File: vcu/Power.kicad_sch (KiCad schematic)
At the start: 21 parts, among them J3 PWR, U11 LD1117S33TR_SOT223, U2 LMR33630CRNX

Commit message: More changes to VCU v2.0.0
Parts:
- added U14: MPS3435GL, symbol SUFST:MP3435GL
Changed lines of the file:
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@@
 		(dnp no)
 		(fields_autoplaced yes)
-		(property "Reference" "#PWR033"
+		(property "Reference" "#PWR0102"
 			(at 198.12 64.77 0)
 			(effects
@@
 			(project "vcu"
 				(path "/d2151cc9-0acc-4d18-a050-63c63ade8261/ef5cbe40-51ae-4964-9d7a-df03e6f84f6f"
-					(reference "#PWR033")
+					(reference "#PWR0102")
 					(unit 1)
 				)
@@
 	)
 	(symbol
+		(lib_id "SUFST:MP3435GL")
+		(at 95.25 95.25 0)
+		(unit 1)
+		(exclude_from_sim no)
+		(in_bom yes)
+		(on_board yes)
+		(dnp no)
+		(property "Reference" "U14"
+			(at 98.806 96.774 0)
+			(effects
+				(font
+					(size 1.27 1.27)
+				)
+			)
+		)
+		(property "Value" "MPS3435GL"
+			(at 99.06 100.076 0)
+			(effects
+				(font
+					(size 1.27 1.27)
+				)
+			)
+		)
+		(property "Footprint" ""
+			(at 95.25 95.25 0)
+			(effects
+				(font
+					(size 1.27 1.27)
+				)
+				(hide yes)
+			)
+		)
+		(property "Datasheet" "https://www.monolithicpower.com/en/documentview/productdocument/index/version/2/document_type/Datasheet/lang/en/sku/MP3435GL"
+			(at 98.806 105.41 0)
+			(effects
+				(font
+					(size 1.27 1.27)
+				)
+				(hide yes)
+			)
+		)
+		(property "Description" ""
+			(at 95.25 95.25 0)
+			(effects
+				(font
+					(size 1.27 1.27)
+				)
+				(hide yes)
+			)
+		)
+		(pin "6"
+		)
+		(pin "10"
+		)
+		(pin "16"
+		)
+		(pin "1"
+		)
+		(pin "11"
+		)
+		(pin "20"
+		)
+		(pin "9"
+		)
+		(pin "7"
+		)
+		(pin "8"
+		)
+		(pin "15"
+		)
+		(pin "19"
+		)
+		(pin "3"
+		)
+		(pin "12"
+		)
+		(pin "17"
+		)
+		(pin "18"
+		)
+		(pin "4"
+		)
+		(pin "5"
+		)
+		(pin "2"
+		)
+		(pin "14"
+		)
+		(pin "13"
+		)
+		(instances
+			(project ""
+				(path "/d2151cc9-0acc-4d18-a050-63c63ade8261/ef5cbe40-51ae-4964-9d7a-df03e6f84f6f"
+					(reference "U14")
+					(unit 1)
+				)
+			)
+		)
+	)
+	(symbol
 		(lib_id "Device:R")
 		(at 242.57 53.34 180)
@@
 		(dnp no)
 		(fields_autoplaced yes)
-		(property "Reference" "#PWR032"
+		(property "Reference" "#PWR0101"
 			(at 242.57 64.77 0)
 			(effects
@@
 			(project "vcu"
 				(path "/d2151cc9-0acc-4d18-a050-63c63ade8261/ef5cbe40-51ae-4964-9d7a-df03e6f84f6f"
-					(reference "#PWR032")
-					(unit 1)
-				)
+					(reference "#PWR0101")
+					(unit 1)
+				)

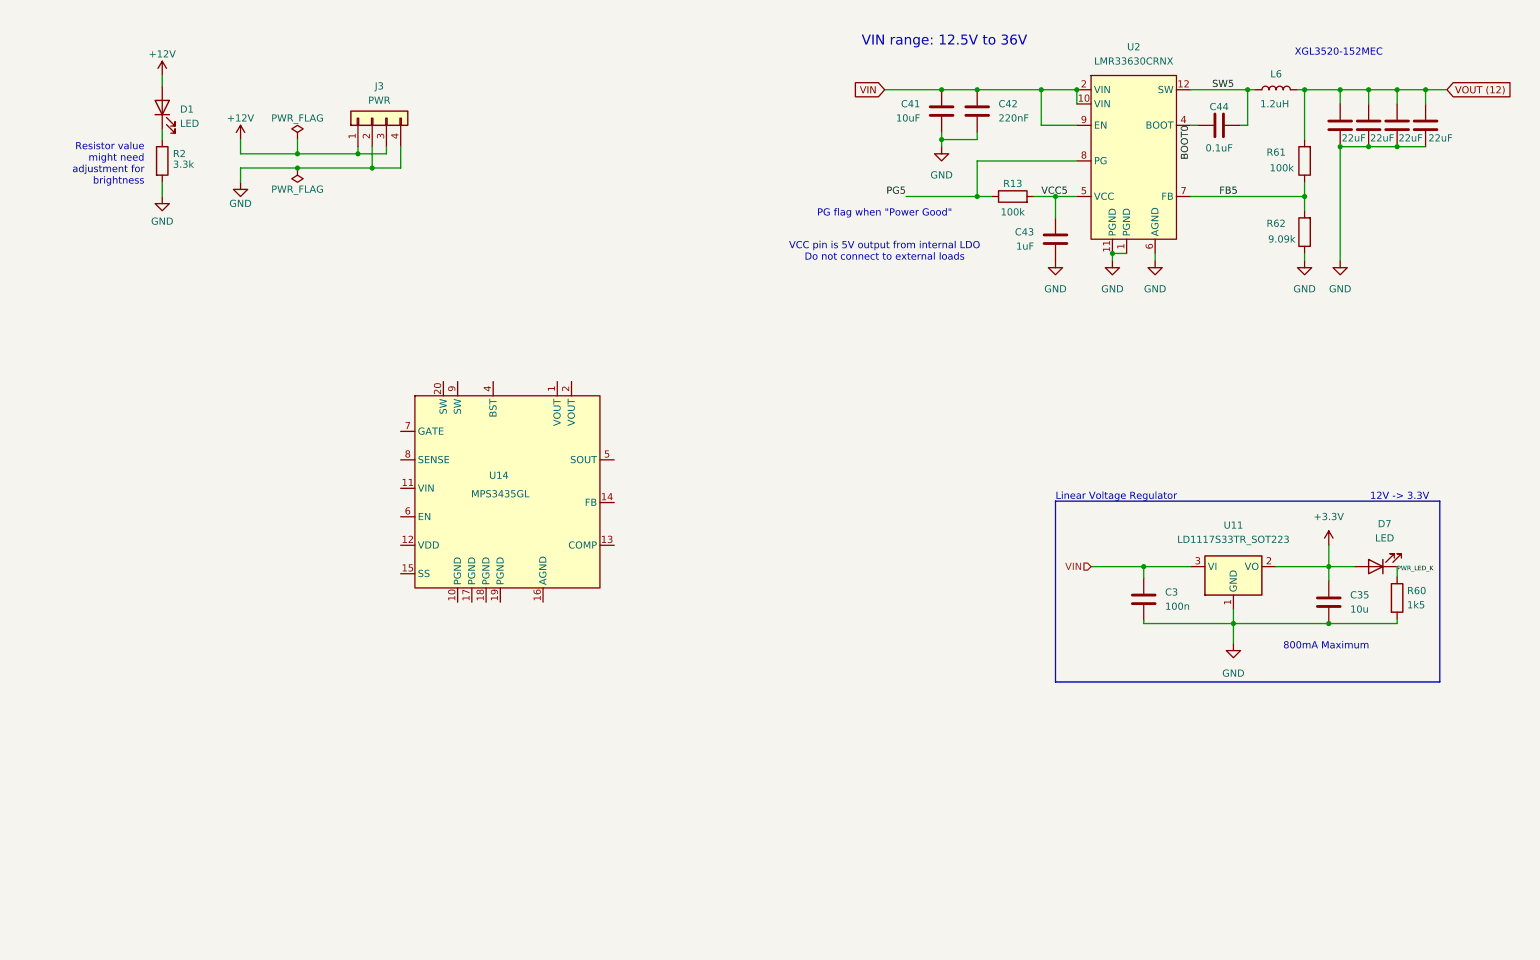
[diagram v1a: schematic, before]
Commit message: Updates to VCU schematic
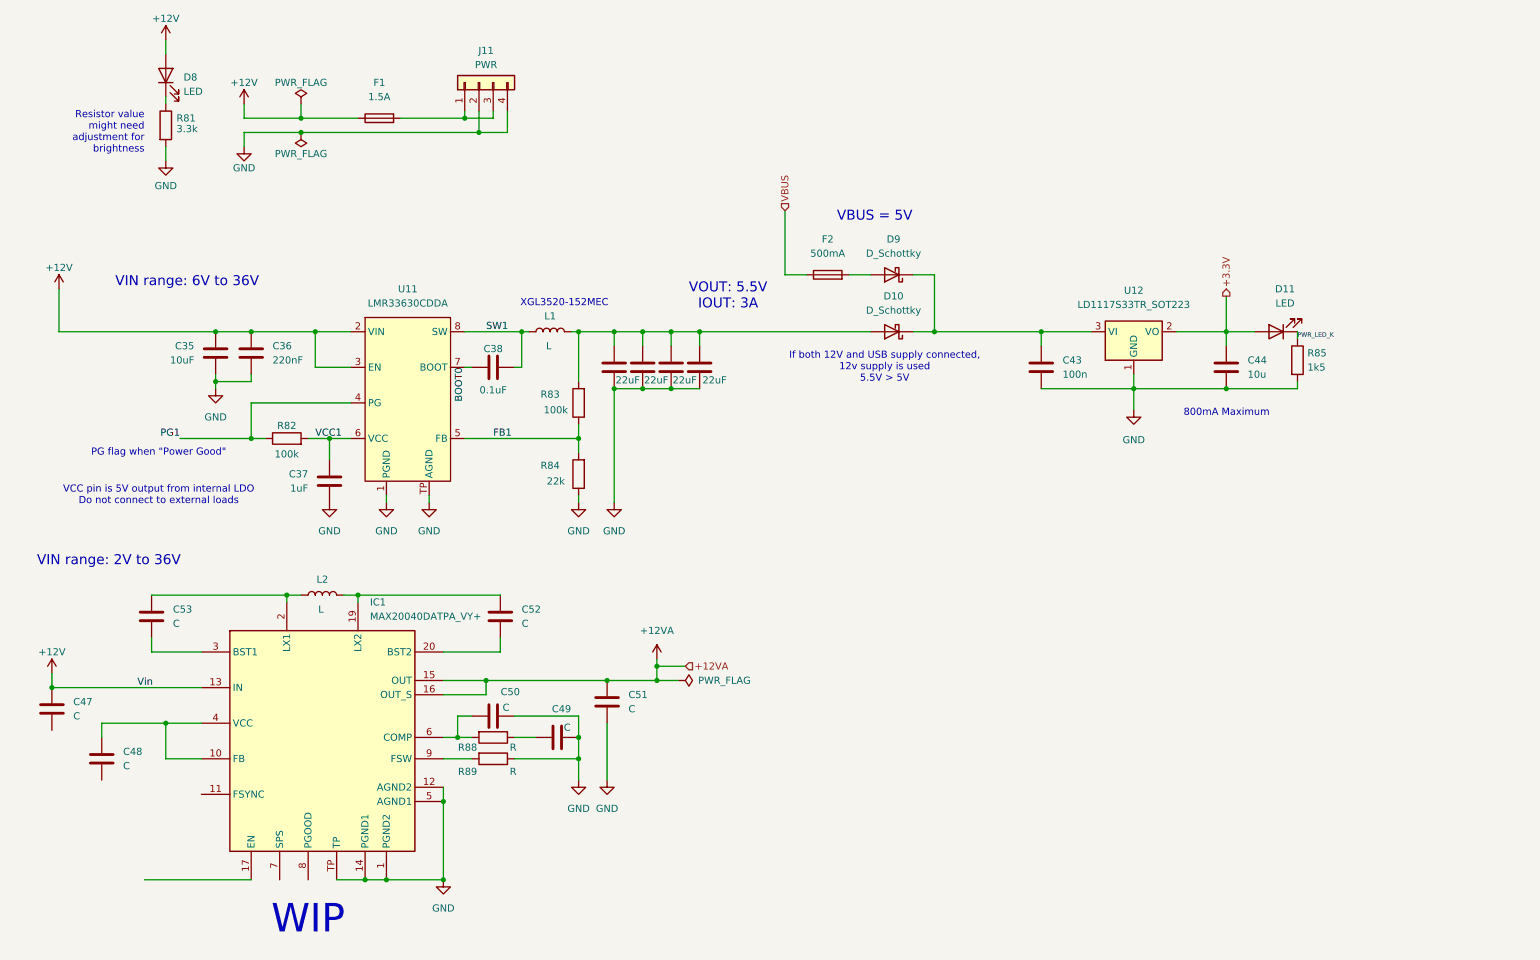
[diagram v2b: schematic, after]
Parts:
- removed C43: 1uF, Capacitor_SMD:C_0603_1608Metric, symbol Device:C
- removed C44: 0.1uF, Capacitor_SMD:C_0603_1608Metric, symbol Device:C
- removed C45, C46: 22uF, Capacitor_SMD:C_0603_1608Metric, symbol Device:C
- removed L6: 1.2uH, SR-Footprint-Library:XGL3520, symbol Device:L
- removed R13, R61: 100k, Resistor_SMD:R_0603_1608Metric, symbol Device:R
- removed R62: 9.09k, Resistor_SMD:R_0603_1608Metric, symbol Device:R
- removed U14: MPS3435GL, symbol SUFST:MP3435GL
- removed U2: LMR33630CRNX, LMR33630CRNX, symbol SR-Symbol-Library:LMR33630CRNX
- added C35: 10uF, Capacitor_SMD:C_0603_1608Metric, symbol Device:C
- added C36: 220nF, Capacitor_SMD:C_0603_1608Metric, symbol Device:C
- added C37: 1uF, Capacitor_SMD:C_0603_1608Metric, symbol Device:C
- added C38: 0.1uF, Capacitor_SMD:C_0603_1608Metric, symbol Device:C
- added C39, C40: 22uF, Capacitor_SMD:C_0603_1608Metric, symbol Device:C
- added C49, C50, C51, C52, C53: C, symbol Device:C
- added D10, D9: D_Schottky, symbol Device:D_Schottky
- added F1: 1.5A, symbol Device:Fuse
- added F2: 500mA, symbol Device:Fuse
- added IC1: MAX20040DATPA_VY+, QFN50P400X400X80-21N-D, symbol SUFST:MAX20040DATPA_VY+
- added L1, L2: L, SR-Footprint-Library:XGL3520, symbol Device:L
- added R82, R83: 100k, Resistor_SMD:R_0603_1608Metric, symbol Device:R
- added R84: 22k, Resistor_SMD:R_0603_1608Metric, symbol Device:R
- added R88, R89: R, symbol Device:R
- added U11: LMR33630CDDA, SR-Footprint-Library:LMR33630CDDA, symbol SR-Symbol-Library:LMR33630CDDA
- C41: value 10uF -> 22uF
- C42: value 220nF -> 22uF
- C47, C48: value 22uF -> C; footprint Capacitor_SMD:C_0603_1608Metric -> (none)
- renumbered C3 to C43, C35 to C44, D7 to D11, D1 to D8, J3 to J11, R2 to R81, R60 to R85, U11 to U12
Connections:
- net +12V: now also C47.1, C35.1, C36.1, F1.1, IC1.13 (IN), U11.2 (VIN), U11.3 (EN); no longer J11.1 (Pin_1), J11.3 (Pin_3)
- net BOOT0: now also C38.1, U11.7 (BOOT)
- net GND: now also C35.2, C36.2, C37.2, C39.2, C40.2, C49.2, C50.2, C51.1, IC1.1 (PGND2), IC1.12 (AGND2), IC1.14 (PGND1), IC1.5 (AGND1), IC1.TP, R84.1, R89.1, U11.1 (PGND), U11.TP (AGND); no longer C47.2, C48.2
- net VIN: no longer names the net of C41.1, C42.1
- net VIN: now also C39.1, C40.1, D10.2 (A), L1.2, R83.2; no longer C43.1, U12.3 (VI)
- net VOUT (12): no longer names the net of C48.1
- net VOUT (12): now also IC1.10 (FB), IC1.4 (VCC); no longer C47.1
- new net: F1.2, J11.1 (Pin_1), J11.3 (Pin_3)
- new net: IC1.9 (FSW), R89.2
- new net: C43.1, D10.1 (K), D9.1 (K), U12.3 (VI)
- new net: C52.2, IC1.19 (LX2), L2.2
- new net: C53.2, IC1.2 (LX1), L2.1
- new net: C52.1, IC1.20 (BST2)
- new net: C53.1, IC1.3 (BST1)
- new net: C50.1, IC1.6 (COMP), R88.2
- new net: C49.1, R88.1
- new net: D9.2 (A), F2.2
- new net +12VA: C51.2, IC1.15 (OUT), IC1.16 (OUT_S)
- new net FB1: R83.1, R84.2, U11.5 (FB)
- new net PG1: R82.1, U11.4 (PG)
- new net SW1: C38.2, L1.1, U11.8 (SW)
- new net VBUS: F2.1
- new net VCC1: C37.1, R82.2, U11.6 (VCC)
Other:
- note added: "If both 12V and USB supply connected, 12v supply is used 5.5V > 5V"
- note added: "VBUS = 5V"
- note added: "VIN range: 2V to 36V"
- note added: "VIN range: 6V to 36V"
- note added: "VOUT: 5.5V IOUT: 3A"
- note added: "WIP"
- note removed: "12V -> 3.3V"
- note removed: "Linear Voltage Regulator"
- note removed: "VIN range: 12.5V to 36V"
- moved on the sheet: C43, C44, D11, D8, J11, R81, R85, U12

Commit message: Streamlined connector allocation
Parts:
- IC1: footprint QFN50P400X400X80-21N-D -> SUFST:QFN50P400X400X80-21N-D
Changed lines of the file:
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@@
 			)
 		)
-		(property "Footprint" "QFN50P400X400X80-21N-D"
+		(property "Footprint" "SUFST:QFN50P400X400X80-21N-D"
 			(at 86.36 167.894 0)
 			(effects
